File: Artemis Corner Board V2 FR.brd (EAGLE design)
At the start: 132.4 x 63.1 mm, 100 parts, among them Q1 BSS138, U1 OPA365AIDBVR, U2 ADS1232IPWR, U3 MCP2562, U4 TM4C123GH6PMI, U5 MCP2562, U6 LM3671MF-3.3/NOPB, U7 LM3671MF-1.2/NOPB, U8 TPS562219, U9 FT232RL, Y1 16MHz, Y2 32.768kHz

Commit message: Playing with layout arrangement
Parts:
- removed C43: 4.7uF, rcl:C0805
- removed C44: 10uF, rcl:C0805
- removed D1, D2: TPD1E05U06, FormE:X2SON
- removed L2: (no value), FormE:0805
- removed R3, R4: 22, rcl:R0805
- removed U7: LM3671MF-1.2/NOPB, FormE:SOT23-5
- added H3: 1-776231-1, FormE:1-776231-1
- H1: value 1-776231-1 -> 776228-4; device FormE:1-776231-1 -> FormE:776228-4
- moved CF2 351.5 mm to (125.7, 3.17), turned to 270 degrees
- moved CF1 349.6 mm to (129.5, 3.17), turned to 270 degrees
- moved C12 345.6 mm to (138.4, 3.17), turned to 270 degrees
- moved C11 344.6 mm to (141.0, 3.17), turned to 270 degrees
- moved C4 344.6 mm to (124.5, -2.54), turned to 270 degrees
- moved C2 343.0 mm to (127.6, -2.54), turned to 270 degrees
- moved R2 341.6 mm to (148.6, 3.17), turned to 270 degrees
- moved C3 341.4 mm to (130.8, -2.54), turned to 270 degrees
- moved R1 339.3 mm to (154.9, 3.17), turned to 270 degrees
- moved U2 333.1 mm to (139.7, -5.71), turned to 270 degrees
- moved C10 332.3 mm to (134.0, -8.26), turned to 90 degrees
- moved C1 330.9 mm to (151.8, -3.81), turned to 270 degrees
- moved JP1 321.5 mm to (142.9, -13.3), turned to 270 degrees
- moved CF4 320.3 mm to (149.9, -12.1), turned to 270 degrees
- moved CF3 318.9 mm to (153.7, -12.1), turned to 270 degrees
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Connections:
- net N$6 renamed VDDC
- removed net +1V2: C44.1, L2.2, U7.4
- removed net N$20: R3.2, R5.1, U1.3
- removed net N$21: Q1.D, R4.2, R6.1
- removed net N$25: L2.1, U7.5
- net +5V: no longer C43.1, U7.1, U7.3
- net ADC_GAIN_BIT_0: now also U4.63; no longer U4.58
- net ADC_GAIN_BIT_1: now also U4.64; no longer U4.57
- net CAR_CAN_N: no longer H1.35
- net CAR_CAN_P: no longer H1.34
- net CAR_CAN_RX: now also U4.28; no longer U4.59
- net CAR_CAN_TX: now also U4.31; no longer U4.60
- net DAMPER_POSITION: now also R5.1, U1.3; no longer D1.I/O, H1.25, R3.1
- net GND: no longer C43.2, C44.2, D1.GND, D2.GND, U7.2
- net IR_SENSOR_CAN_N: no longer H1.12
- net IR_SENSOR_CAN_P: no longer H1.11
- net N$15: now also Y2.1; no longer Y2.2
- net N$17: now also Y2.2; no longer Y2.1
- net STRAIN_GAUGE_NEGATIVE: no longer H1.26
- net STRAIN_GAUGE_POSITIVE: no longer H1.28
- net WHEEL_TACHOMETER: now also Q1.D, R6.1; no longer D2.I/O, H1.24, R4.1
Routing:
- net GND: track 0.00 -> 10.4 mm, vias 0 -> 6
- net +3V3: track 0.00 -> 1.74 mm, vias 0 -> 1

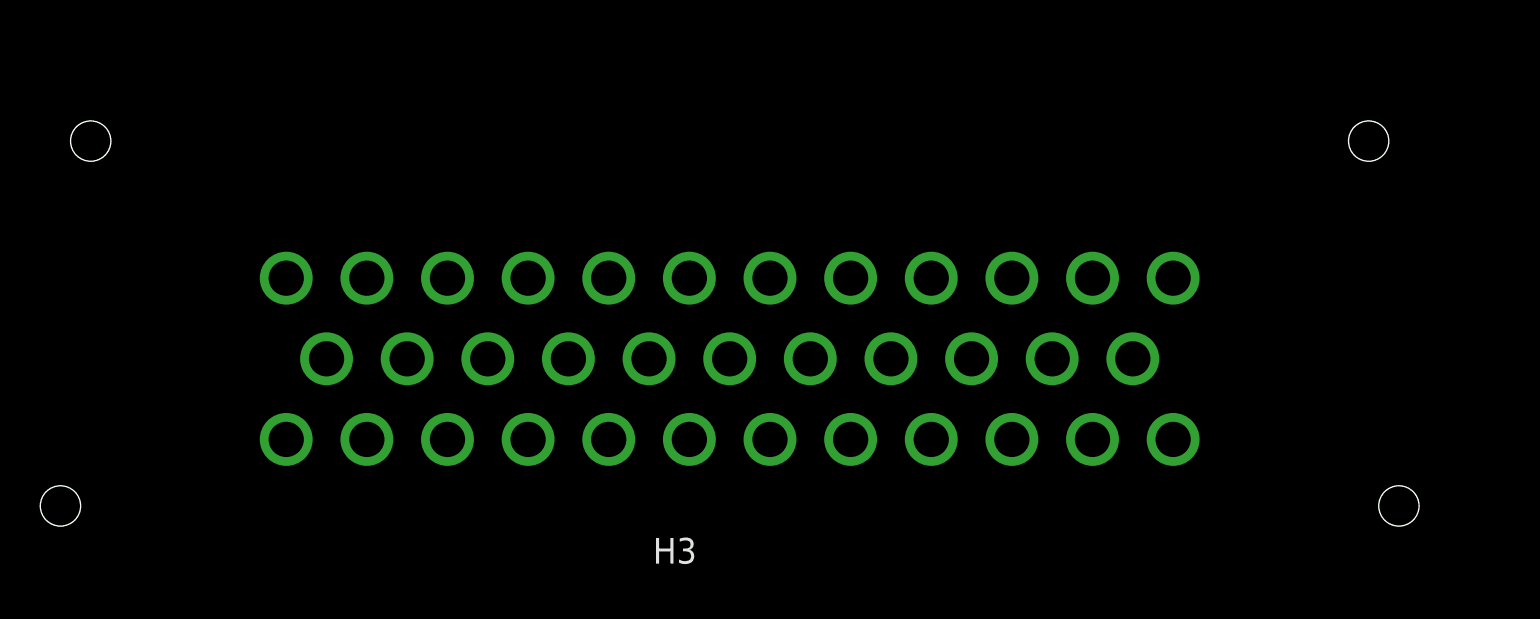
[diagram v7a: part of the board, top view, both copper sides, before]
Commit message: Switched to 23-pin ampseal connector
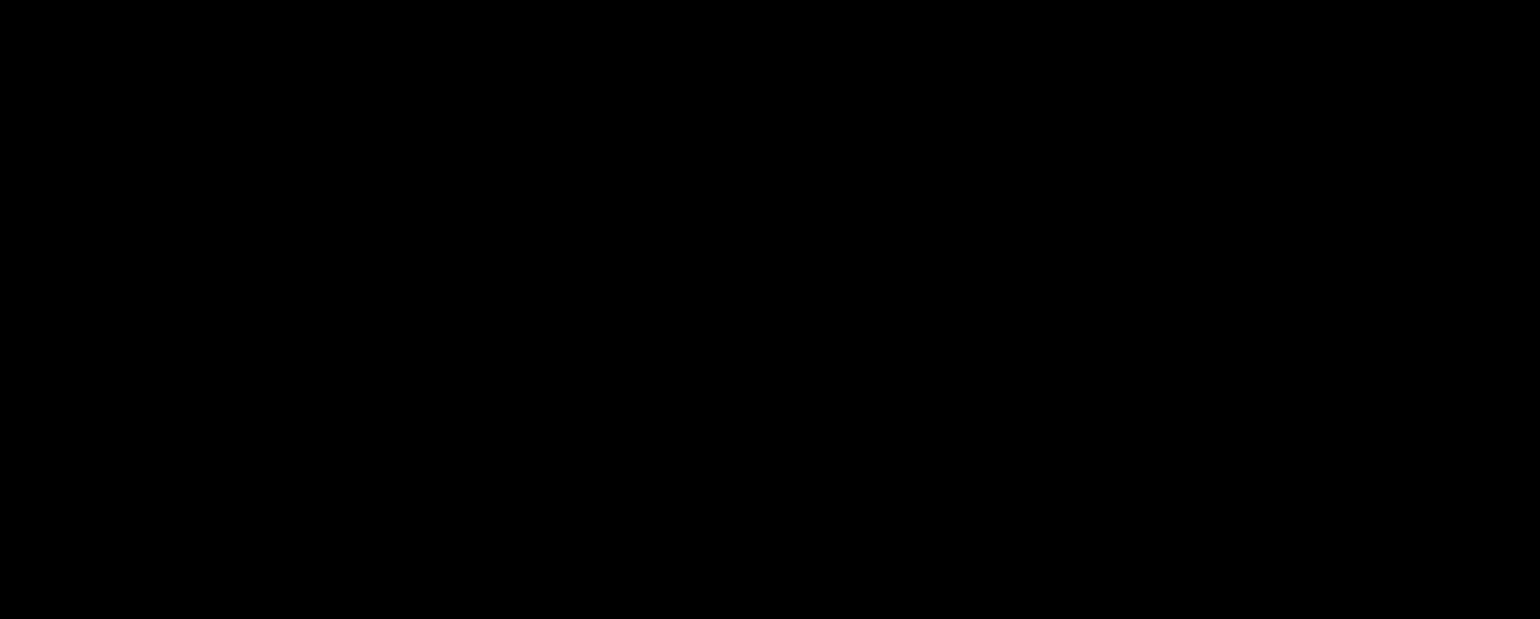
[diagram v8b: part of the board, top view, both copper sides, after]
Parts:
- removed H3: 1-776231-1, FormE:1-776231-1
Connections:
- net +5V: now also H1.P$12, H1.P$13, H1.P$2, H1.P$7
- net CAR_CAN_N: now also H1.P$17
- net CAR_CAN_P: now also H1.P$16
- net DAMPER_POSITION: now also H1.P$3
- net GND: now also H1.P$10, H1.P$11, H1.P$14, H1.P$21, H1.P$9
- net IR_SENSOR_CAN_N: now also H1.P$19
- net IR_SENSOR_CAN_P: now also H1.P$18
- net STRAIN_GAUGE_NEGATIVE: now also H1.P$15
- net STRAIN_GAUGE_POSITIVE: now also H1.P$8
- net VCC: now also H1.P$1
- net WHEEL_TACHOMETER: now also H1.P$20
